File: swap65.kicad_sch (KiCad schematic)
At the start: 35 parts, among them J1 USB_C_Receptacle_USB2.0, J2 OLED, J3 DB, SW1 SW_Push, SW2 SW_Push, U1 RP2040, U2 SRV05-4, U3 W25Q128JVS, U4 XC6206PxxxMR, Y1 12MHz

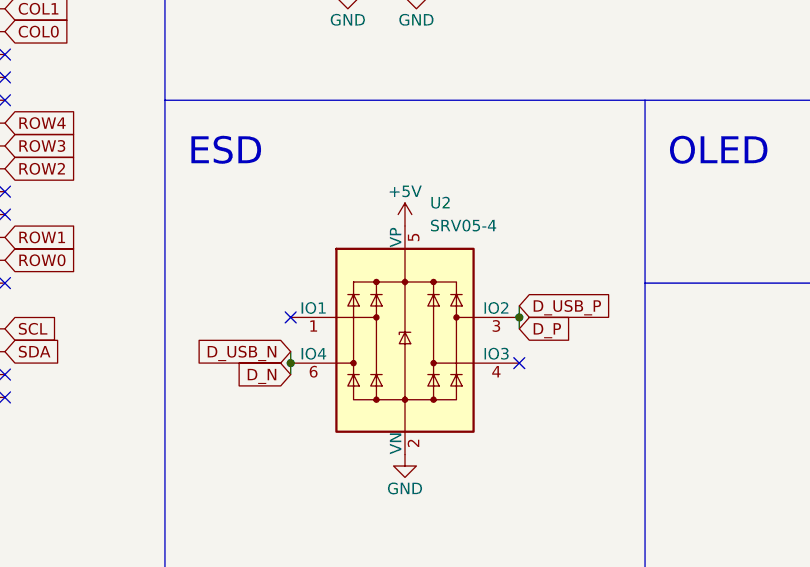
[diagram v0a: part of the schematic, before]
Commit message: routed usb and jst connector
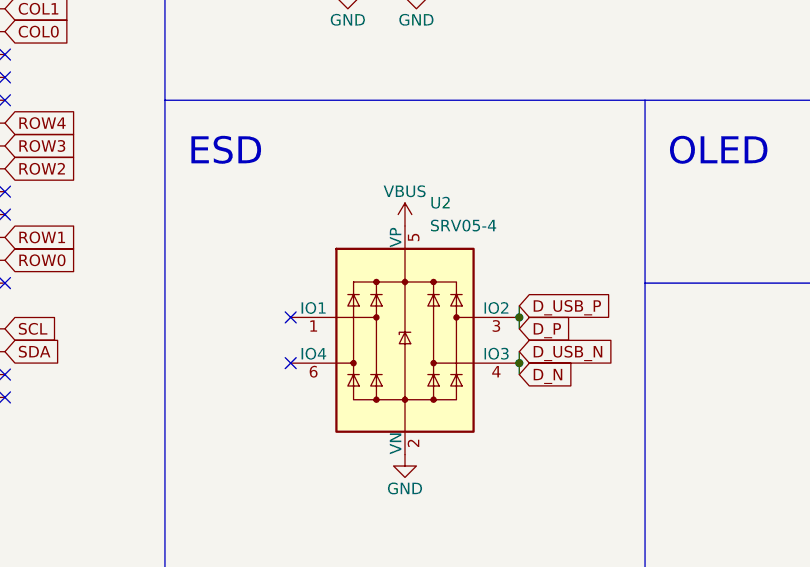
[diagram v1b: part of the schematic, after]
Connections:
- net +5V: no longer U2.5 (VP)
- net D_N: now also U2.4 (IO3); no longer U2.6 (IO4)
- net VBUS: now also U2.5 (VP)
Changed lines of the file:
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@@
   (junction (at 169.545 87.63) (diameter 0) (color 0 0 0 0)
   )
+  (junction (at 161.29 172.72) (diameter 0) (color 0 0 0 0)
+  )
   (junction (at 30.48 36.83) (diameter 0) (color 0 0 0 0)
   )
@@
   (junction (at 182.88 87.63) (diameter 0) (color 0 0 0 0)
   )
-  (junction (at 135.89 172.72) (diameter 0) (color 0 0 0 0)
-  )
   (junction (at 165.1 87.63) (diameter 0) (color 0 0 0 0)
   )
@@
   (junction (at 101.6 44.45) (diameter 0) (color 0 0 0 0)
   )
-  (no_connect (at 161.29 172.72))
   (no_connect (at 104.14 153.67))
   (no_connect (at 135.89 167.64))
@@
   (no_connect (at 165.1 118.11))
   (no_connect (at 104.14 140.97))
+  (no_connect (at 135.89 172.72))
   (no_connect (at 104.14 138.43))
   (no_connect (at 104.14 176.53))
@@
     (stroke (width 0) (type default) (color 0 0 0 0))
   )
+  (wire (pts (xy 161.29 172.72) (xy 161.29 173.99))
+    (stroke (width 0) (type default) (color 0 0 0 0))
+  )
   (wire (pts (xy 142.24 39.37) (xy 152.4 39.37))
     (stroke (width 0) (type default) (color 0 0 0 0))
@@
     (stroke (width 0) (type default) (color 0 0 0 0))
   )
-  (wire (pts (xy 135.89 171.45) (xy 135.89 172.72))
+  (wire (pts (xy 161.29 171.45) (xy 161.29 172.72))
     (stroke (width 0) (type default) (color 0 0 0 0))
   )
@@
   )
   (polyline (pts (xy 13.97 13.97) (xy 13.97 64.77))
-    (stroke (width 0) (type default) (color 0 0 0 0))
-  )
-  (wire (pts (xy 135.89 172.72) (xy 135.89 173.99))
     (stroke (width 0) (type default) (color 0 0 0 0))
   )
@@
     )
   )
-  (global_label "D_USB_N" (shape input) (at 135.89 171.45 180) (fields_autoplaced)
-    (effects (font (size 1.27 1.27)) (justify right))
-    (property "Intersheet References" "${INTERSHEET_REFS}" (id 0) (at 125.1312 171.5294 0)
-      (effects (font (size 1.27 1.27)) (justify right) hide)
+  (global_label "D_USB_N" (shape input) (at 161.29 171.45 0) (fields_autoplaced)
+    (effects (font (size 1.27 1.27)) (justify left))
+    (property "Intersheet References" "${INTERSHEET_REFS}" (id 0) (at 172.0488 171.3706 0)
+      (effects (font (size 1.27 1.27)) (justify left) hide)
     )
   )
@@
     )
   )
-  (global_label "D_N" (shape input) (at 135.89 173.99 180) (fields_autoplaced)
-    (effects (font (size 1.27 1.27)) (justify right))
-    (property "Intersheet References" "${INTERSHEET_REFS}" (id 0) (at 129.9088 174.0694 0)
-      (effects (font (size 1.27 1.27)) (justify right) hide)
+  (global_label "D_N" (shape input) (at 161.29 173.99 0) (fields_autoplaced)
+    (effects (font (size 1.27 1.27)) (justify left))
+    (property "Intersheet References" "${INTERSHEET_REFS}" (id 0) (at 167.2712 173.9106 0)
+      (effects (font (size 1.27 1.27)) (justify left) hide)
     )
   )
@@
     )
     (property "Datasheet" "" (id 3) (at 48.26 36.83 0)
+      (effects (font (size 1.27 1.27)) hide)
+    )
+    (pin "1")
+  )
+  (symbol (lib_id "power:VBUS") (at 148.59 157.48 0) (unit 1)
+    (in_bom yes) (on_board yes)
+    (property "Reference" "#PWR?" (id 0) (at 148.59 161.29 0)
+      (effects (font (size 1.27 1.27)) hide)
+    )
+    (property "Value" "VBUS" (id 1) (at 148.59 153.67 0))
+    (property "Footprint" "" (id 2) (at 148.59 157.48 0)
+      (effects (font (size 1.27 1.27)) hide)
+    )
+    (property "Datasheet" "" (id 3) (at 148.59 157.48 0)
       (effects (font (size 1.27 1.27)) hide)
     )
@@
     (pin "S1")
   )
-  (symbol (lib_id "power:+5V") (at 148.59 157.48 0) (unit 1)
-    (in_bom yes) (on_board yes)
-    (property "Reference" "#PWR014" (id 0) (at 148.59 161.29 0)
-      (effects (font (size 1.27 1.27)) hide)
-    )
-    (property "Value" "+5V" (id 1) (at 148.59 153.67 0))
-    (property "Footprint" "" (id 2) (at 148.59 157.48 0)
-      (effects (font (size 1.27 1.27)) hide)
-    )
-    (property "Datasheet" "" (id 3) (at 148.59 157.48 0)
-      (effects (font (size 1.27 1.27)) hide)
-    )
-    (pin "1")
-  )
   (symbol (lib_id "Device:C_Small") (at 38.1 40.64 0) (unit 1)
     (in_bom yes) (on_board yes)
@@
       (reference "#PWR013") (unit 1) (value "GND") (footprint "")
     )
-    (path "/f149d317-4170-462d-b82e-16b2e3d8dde1"
-      (reference "#PWR014") (unit 1) (value "+5V") (footprint "")
-    )
     (path "/e911e012-8ef6-436e-81e0-88416fa9c221"
       (reference "#PWR015") (unit 1) (value "GND") (footprint "")
@@
       (reference "#PWR0102") (unit 1) (value "GND") (footprint "")
     )
+    (path "/2312ddd4-45e2-4bdc-bde0-23b8a7c61a39"
+      (reference "#PWR?") (unit 1) (value "VBUS") (footprint "")
+    )
     (path "/ceb4ec2e-d6e1-4ebf-b055-b68396bb9943"

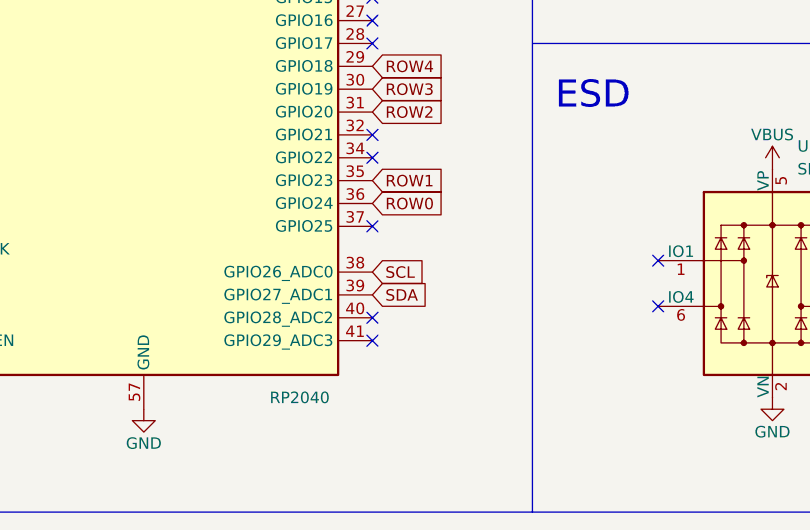
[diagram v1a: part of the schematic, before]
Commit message: routed mcu
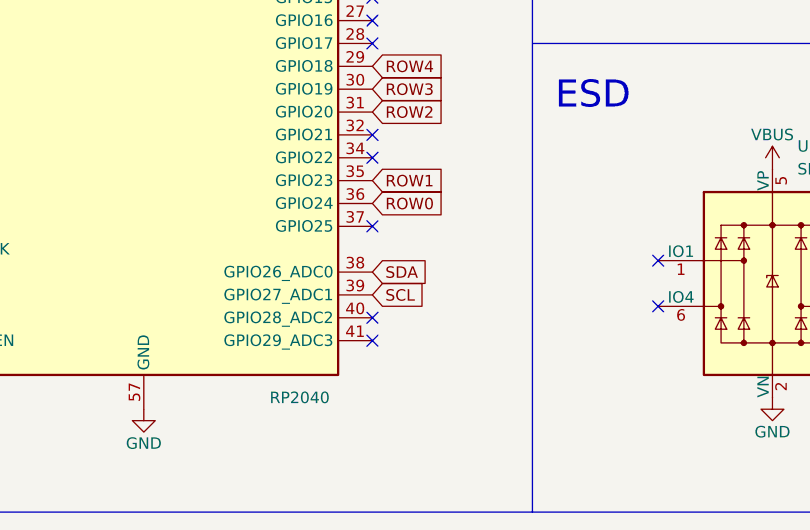
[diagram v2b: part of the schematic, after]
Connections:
- net SCL: now also U1.39 (GPIO27_ADC1); no longer U1.38 (GPIO26_ADC0)
- net SDA: now also U1.38 (GPIO26_ADC0); no longer U1.39 (GPIO27_ADC1)
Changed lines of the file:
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@@
     )
   )
-  (global_label "SCL" (shape input) (at 104.14 168.91 0) (fields_autoplaced)
-    (effects (font (size 1.27 1.27)) (justify left))
-    (property "Intersheet References" "${INTERSHEET_REFS}" (id 0) (at 110.0607 168.9894 0)
+  (global_label "SCL" (shape input) (at 104.14 171.45 0) (fields_autoplaced)
+    (effects (font (size 1.27 1.27)) (justify left))
+    (property "Intersheet References" "${INTERSHEET_REFS}" (id 0) (at 110.0607 171.5294 0)
       (effects (font (size 1.27 1.27)) (justify left) hide)
     )
@@
     )
   )
-  (global_label "SDA" (shape input) (at 104.14 171.45 0) (fields_autoplaced)
-    (effects (font (size 1.27 1.27)) (justify left))
-    (property "Intersheet References" "${INTERSHEET_REFS}" (id 0) (at 110.1212 171.5294 0)
+  (global_label "SDA" (shape input) (at 104.14 168.91 0) (fields_autoplaced)
+    (effects (font (size 1.27 1.27)) (justify left))
+    (property "Intersheet References" "${INTERSHEET_REFS}" (id 0) (at 110.1212 168.9894 0)
       (effects (font (size 1.27 1.27)) (justify left) hide)
     )
@@
   (symbol (lib_id "power:VBUS") (at 148.59 157.48 0) (unit 1)
     (in_bom yes) (on_board yes)
-    (property "Reference" "#PWR?" (id 0) (at 148.59 161.29 0)
+    (property "Reference" "#PWR0103" (id 0) (at 148.59 161.29 0)
       (effects (font (size 1.27 1.27)) hide)
     )
@@
     )
     (path "/2312ddd4-45e2-4bdc-bde0-23b8a7c61a39"
-      (reference "#PWR?") (unit 1) (value "VBUS") (footprint "")
+      (reference "#PWR0103") (unit 1) (value "VBUS") (footprint "")
     )
     (path "/ceb4ec2e-d6e1-4ebf-b055-b68396bb9943"

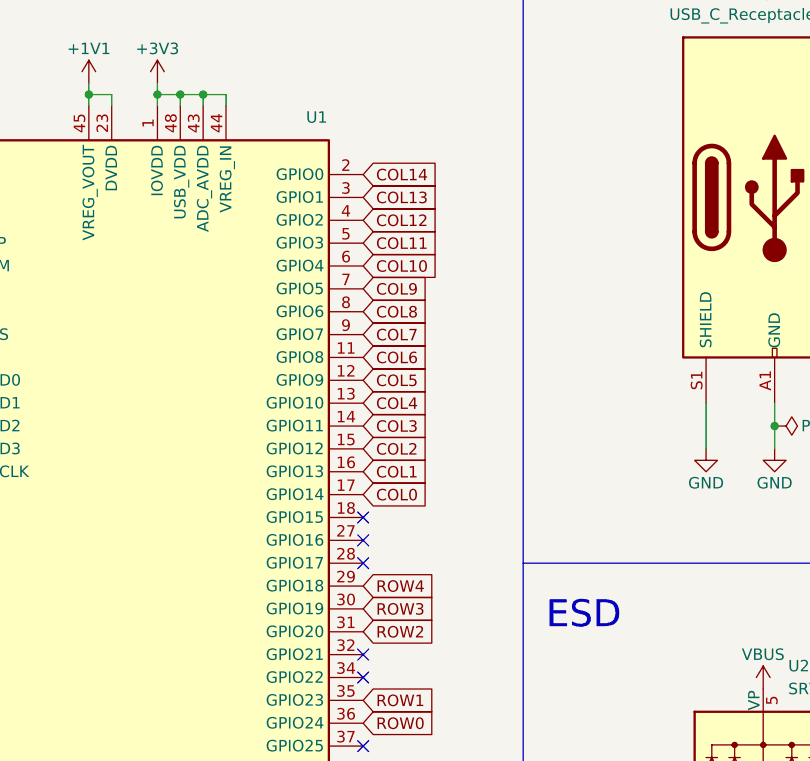
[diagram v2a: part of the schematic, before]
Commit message: second pass at routing complete
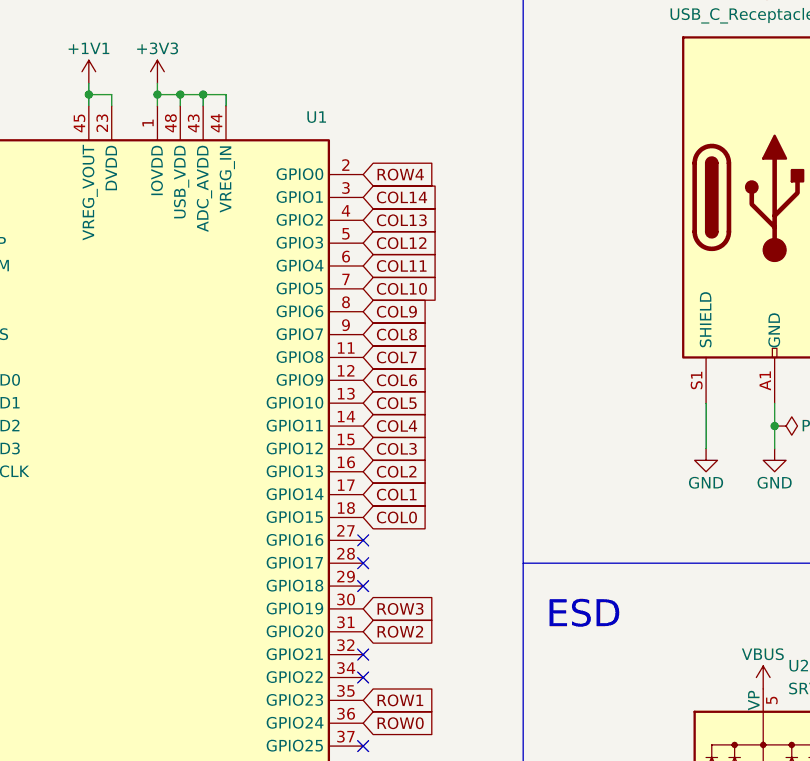
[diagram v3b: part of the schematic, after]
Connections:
- net COL0: now also U1.18 (GPIO15); no longer U1.17 (GPIO14)
- net COL1: now also U1.17 (GPIO14); no longer U1.16 (GPIO13)
- net COL10: now also U1.7 (GPIO5); no longer U1.6 (GPIO4)
- net COL11: now also U1.6 (GPIO4); no longer U1.5 (GPIO3)
- net COL12: now also U1.5 (GPIO3); no longer U1.4 (GPIO2)
- net COL13: now also U1.4 (GPIO2); no longer U1.3 (GPIO1)
- net COL14: now also U1.3 (GPIO1); no longer U1.2 (GPIO0)
- net COL2: now also U1.16 (GPIO13); no longer U1.15 (GPIO12)
- net COL3: now also U1.15 (GPIO12); no longer U1.14 (GPIO11)
- net COL4: now also U1.14 (GPIO11); no longer U1.13 (GPIO10)
- net COL5: now also U1.13 (GPIO10); no longer U1.12 (GPIO9)
- net COL6: now also U1.12 (GPIO9); no longer U1.11 (GPIO8)
- net COL7: now also U1.11 (GPIO8); no longer U1.9 (GPIO7)
- net COL8: now also U1.9 (GPIO7); no longer U1.8 (GPIO6)
- net COL9: now also U1.8 (GPIO6); no longer U1.7 (GPIO5)
- net ROW4: now also U1.2 (GPIO0); no longer U1.29 (GPIO18)
